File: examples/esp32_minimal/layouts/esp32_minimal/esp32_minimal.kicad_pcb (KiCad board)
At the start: 2 copper layers, 36.2 x 26.8 mm, 20 parts

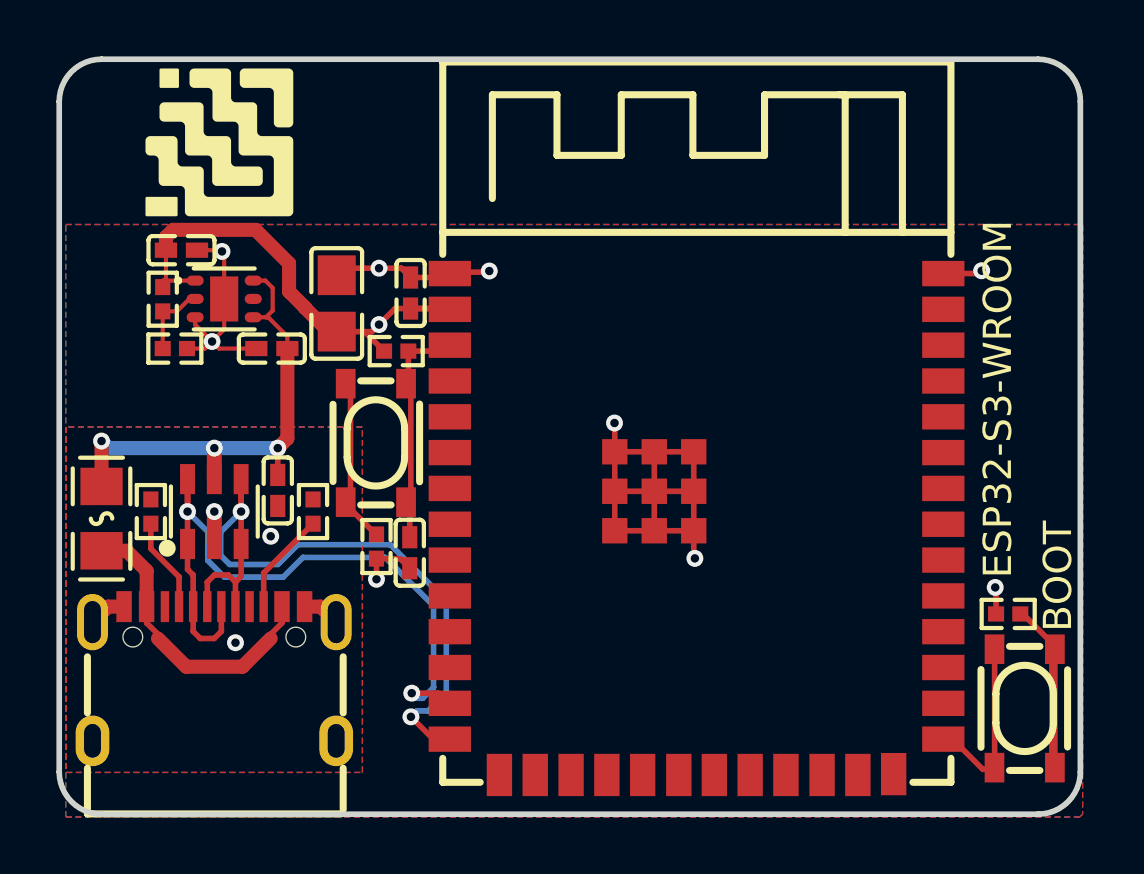
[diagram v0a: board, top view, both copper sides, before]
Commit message: Restore Atopile Local 0.2 on pinned 0.15.9 sources
Import the publicly distributed atopile 0.15.9 PyPI source release as the
compiler/UI baseline, retaining upstream main as its historical parent.
PyPI source SHA256: 681cc1e123646dd133de31b631aedaf4eaac88682613b4f82d1da4b3ef8b4e8e.

Revive the local VS Code extension with a separate identity and launcher,
isolated state, bundled visualization assets, and provider settings. Bridge
the existing Atopile tool harness to a natively signed-in Codex app-server
for ChatGPT-plan use, retaining direct API providers as explicit options.
Include local part import, layout tools, packaging/runtime setup and tests.

Preserve upstream licensing, restored GitHub metadata and source notices.
Exclude local environments, generated webview bundles and personal QA paths.
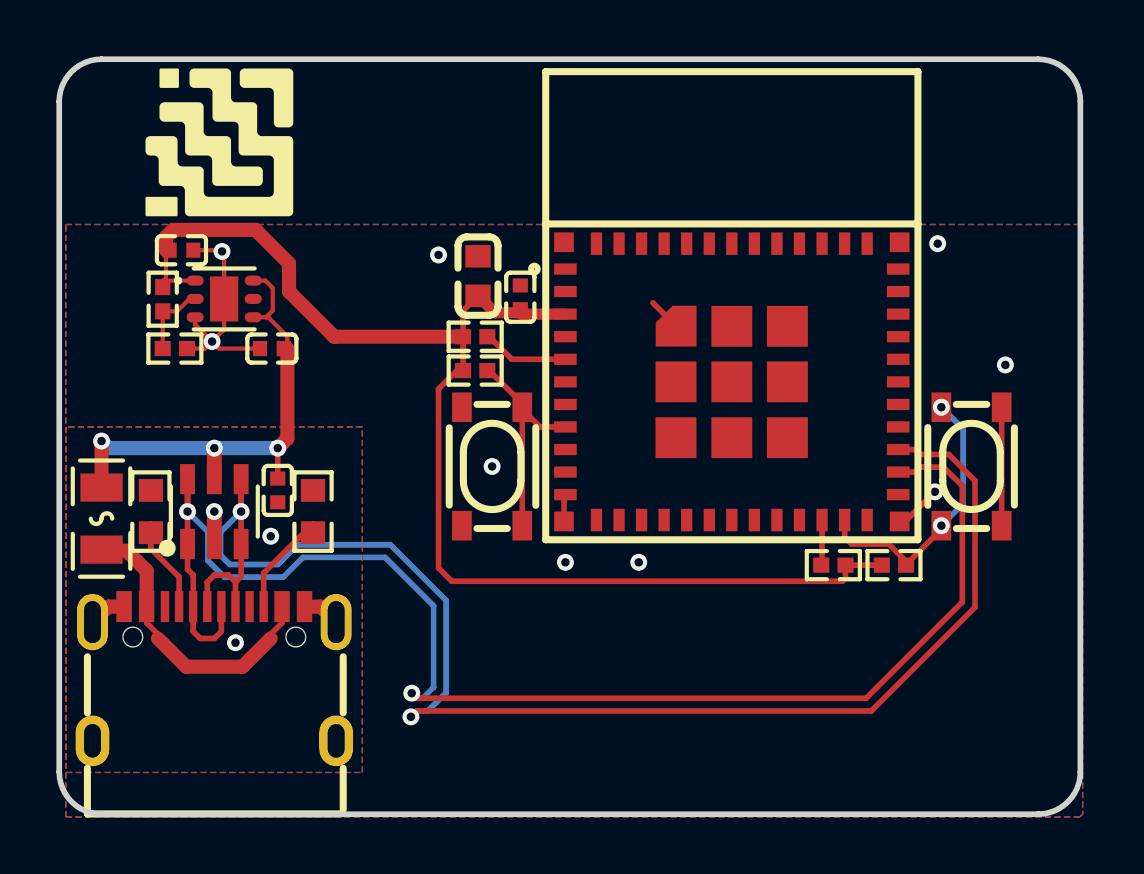
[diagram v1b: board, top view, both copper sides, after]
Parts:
- removed C10: 1µF ±10% 25V X5R, Samsung_Electro_Mechanics_CL05A105KA5NQNC:C0402
- removed C8: 100nF ±10% 16V X7R, Samsung_Electro_Mechanics_CL05B104KO5NNNC:C0402
- removed C9: 22µF ±20% 6.3V X5R, Samsung_Electro_Mechanics_CL21A226MQQNNNE:C0805
- removed U2: , Espressif_Systems_ESP32_S3_WROOM_1_N8R8:WIRELM-SMD_ESP32-S3-WROOM-1
- added C4: 22µF ±20%, Samsung_Electro_Mechanics_CL10A226MQ8NRNC:C0603, F.Cu at (144.1, 118.7)
- added C5: 100nF ±10%, Samsung_Electro_Mechanics_CL05B104KO5NNNC:C0402, F.Cu at (145.6, 119.4)
- added R8: 10kΩ ±1%, UNI_ROYAL_0402WGF1002TCE:R0402, F.Cu at (144.0, 122.0)
- added U1: , Espressif_Systems_ESP32_C3_MINI_1_N4:WIFIM-SMD_ESP32-C3-MINI-1, F.Cu at (153.1, 122.4)
- C1, C2: value 1µF ±10% 25V X5R -> 1µF ±10%
- C3: value 100nF ±10% 16V X7R -> 100nF ±10%
- R1: value 10kΩ ±1% 62.5mW -> 9.09kΩ ±1%; footprint UNI_ROYAL_0402WGF1002TCE:R0402 -> UNI_ROYAL_0402WGF9091TCE:R0402
- R2: value 100Ω ±1% 62.5mW -> 1.82kΩ ±1%; footprint UNI_ROYAL_0402WGF1000TCE:R0402 -> KOA_Speer_Elec_RK73H1ETTP1821F:R0402
- R3: value 10kΩ ±1% 62.5mW -> 10kΩ ±1%
- R4: value 100Ω ±1% 62.5mW -> 10kΩ ±1%; footprint UNI_ROYAL_0402WGF1000TCE:R0402 -> UNI_ROYAL_0402WGF1002TCE:R0402
- R5: value 47kΩ ±1% 62.5mW -> 5.1kΩ ±1%; footprint UNI_ROYAL_0402WGF4702TCE:R0402 -> UNI_ROYAL_0402WGF5101TCE:R0402
- R6, R7: value 5.1kΩ ±1% 62.5mW -> 10kΩ ±1%; footprint UNI_ROYAL_0402WGF5101TCE:R0402 -> UNI_ROYAL_0603WAF1002T5E:R0603
- moved R2 31.0 mm to (133.3, 121.2), turned to 0 degrees
- moved R5 27.6 mm to (158.8, 128.9), turned to 0 degrees
- moved R4 16.2 mm to (156.7, 128.9), turned to 0 degrees
- moved SW1 8.78 mm to (161.6, 125.4)
- moved SW2 4.21 mm to (144.6, 125.4)
- moved R3 2.85 mm to (144.0, 120.8)
- moved R1 1.80 mm to (132.9, 119.5), turned to -90 degrees
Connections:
- net USB_D_N renamed DATA_N
- net USB_D_P renamed DATA_P
- net cc[0]-line renamed 4
- net cc[1]-line renamed 10
- net power_in-VCC renamed hv
- net power_vbus-VCC renamed power_vbus-hv
- net sbu[0]-line renamed 9
- net sbu[1]-line renamed 3
- C1 pad 2: GND -> lv
- C2 pad 1: power-VCC -> power-hv
- C2 pad 2: GND -> lv
- C3 pad 2: GND -> lv
- D1 pad 2: GND -> lv
- R1 pad 1: VDIV_OUTPUT -> power-hv
- R1 pad 2: GND -> ref_out-hv
- R2 pad 1: button-input-input-0 -> ref_out-hv
- R2 pad 2: GND -> lv
- R3 pad 1: output-output -> DATA_1
- R3 pad 2: power-VCC -> power-hv
- R4 pad 1: button-input-input-1 -> MISO
- R4 pad 2: GND -> power-hv
- R5 pad 1: power-VCC -> power-hv
- R5 pad 2: VDIV_OUTPUT -> output
- R6 pad 2: GND -> lv
- R7 pad 2: GND -> lv
- SW1 pad 1: button-input-input-0 -> lv
- SW1 pad 2: button-input-input-0 -> lv
- SW1 pad 3: gpios[0]-output -> output
- SW1 pad 4: gpios[0]-output -> output
- SW2 pad 1: button-input-input-1 -> lv
- SW2 pad 2: button-input-input-1 -> lv
- SW2 pad 3: output-output -> N_TRST
- SW2 pad 4: output-output -> N_TRST
- U3 pad 1: power-VCC -> power-hv
- U3 pad 2: VDIV_OUTPUT -> ref_out-hv
- U3 pad 3: GND -> lv
- U3 pad 7: GND -> lv
- USB1 pad : net -> (no net)
- USB1 pad 1: GND -> lv
- USB1 pad 12: GND -> lv
- USB1 pad 13: GND -> lv
- USB1 pad 14: GND -> lv
- USB1 pad 15: GND -> lv
- USB1 pad 16: GND -> lv
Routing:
- net power-hv: track 0.00 -> 46.2 mm
- net GND: track 41.0 -> 0.00 mm, vias 12 -> 0
- net DATA_P: track 25.4 -> 53.1 mm
- net DATA_N: track 25.3 -> 51.7 mm
- net lv: track 0.00 -> 19.9 mm, vias 0 -> 10
- net power-VCC: track 18.1 -> 0.00 mm, vias 1 -> 0
- net button-input-input-0: track 10.3 -> 0.00 mm
- net output: track 0.00 -> 10.1 mm, vias 0 -> 2
- net output-output: track 8.21 -> 0.00 mm
- net N_TRST: track 0.00 -> 7.92 mm
- net gpios[0]-output: track 6.46 -> 0.00 mm
- net button-input-input-1: track 5.75 -> 0.00 mm
- net DATA_1: track 0.00 -> 3.10 mm
- net ref_out-hv: track 0.00 -> 2.65 mm
- net VDIV_OUTPUT: track 2.65 -> 0.00 mm
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- added copper zone on B.Cu, net lv
- added copper zone on F.Cu, net lv
- removed copper zone on B.Cu, net GND
- removed copper zone on F.Cu, net GND
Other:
- board text removed: "BOOT"
- board text removed: "ESP32-S3-WROOM"
